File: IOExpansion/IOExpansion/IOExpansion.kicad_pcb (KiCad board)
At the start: 2 copper layers, 155 x 114 mm, 61 parts, among them J1 Mount_Hole_3.2mm_M3, J10 HEADER 2x20, J11 I2C_5V, J12 I2C_3V3, J13 I2C_ALT_Master, J14 I2C_Debug, J2 Mount_Hole_3.2mm_M3, J3 Mount_Hole_3.2mm_M3, J4 Mount_Hole_3.2mm_M3, J5 UART_5V, J6 GPIO_3V3, J7 RTC_SQW, J8 I2C_INT, J9 SPI _3V3, U1 MCP810-450, U10 PCA9641, U11 SC18IS602B, U12 PCA9517A, U13 PCA9517A, U14 MCP809-450, U15 LM3671_Breakout, U2 MCP809-315, U3 SG-8002DC, U4 PC16550D, U5 TXB0104_Breakout, U6 PCA9632DP1_Breakout, U7 GAL16V8, U8 SC18IM700, U9 PCF8523_Breakout

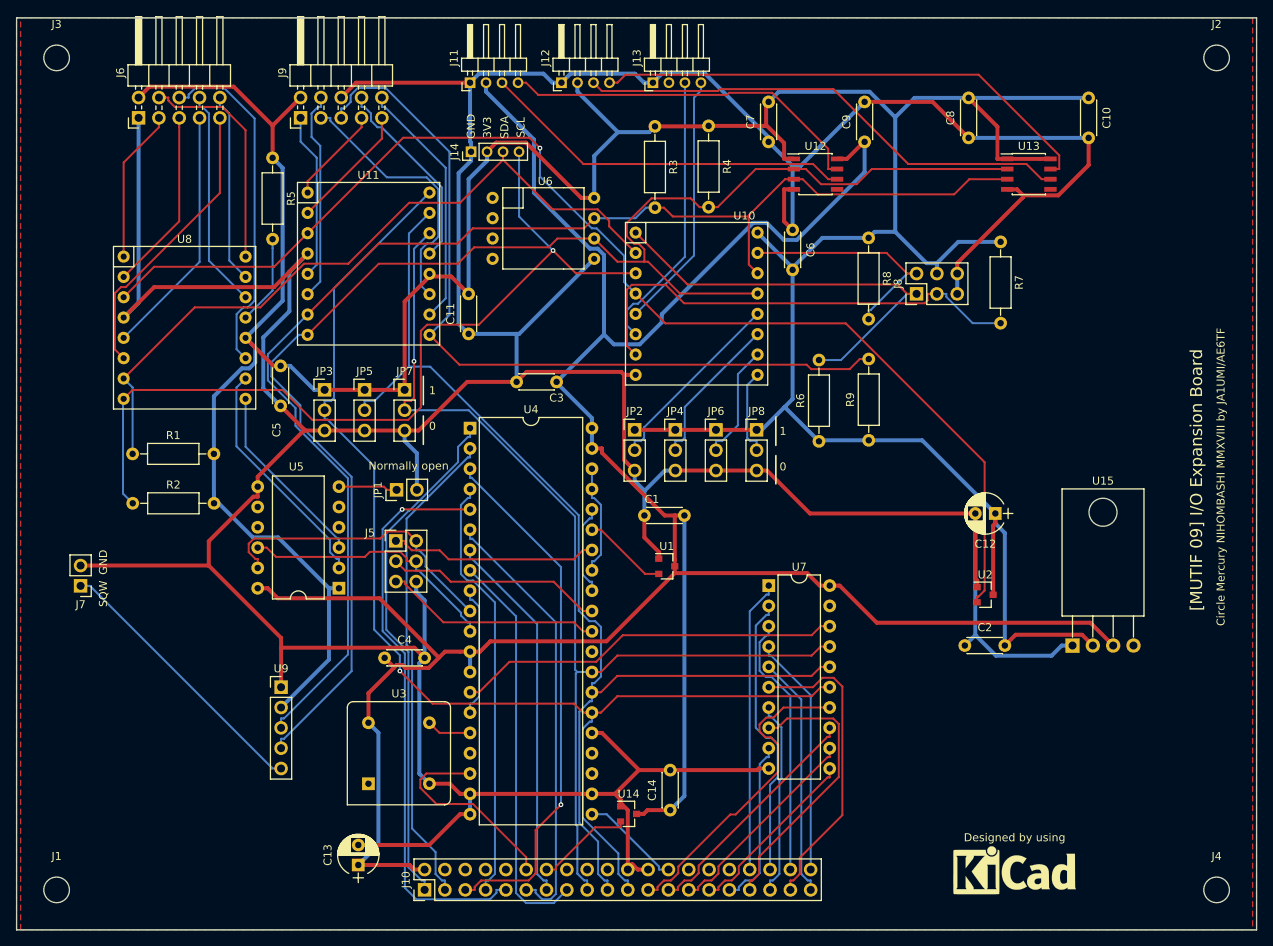
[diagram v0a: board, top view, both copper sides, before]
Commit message: Update files for MUTIF09 I/O Expansion Board (Revision 3). Functionality tests were completed on May 21, 2019.
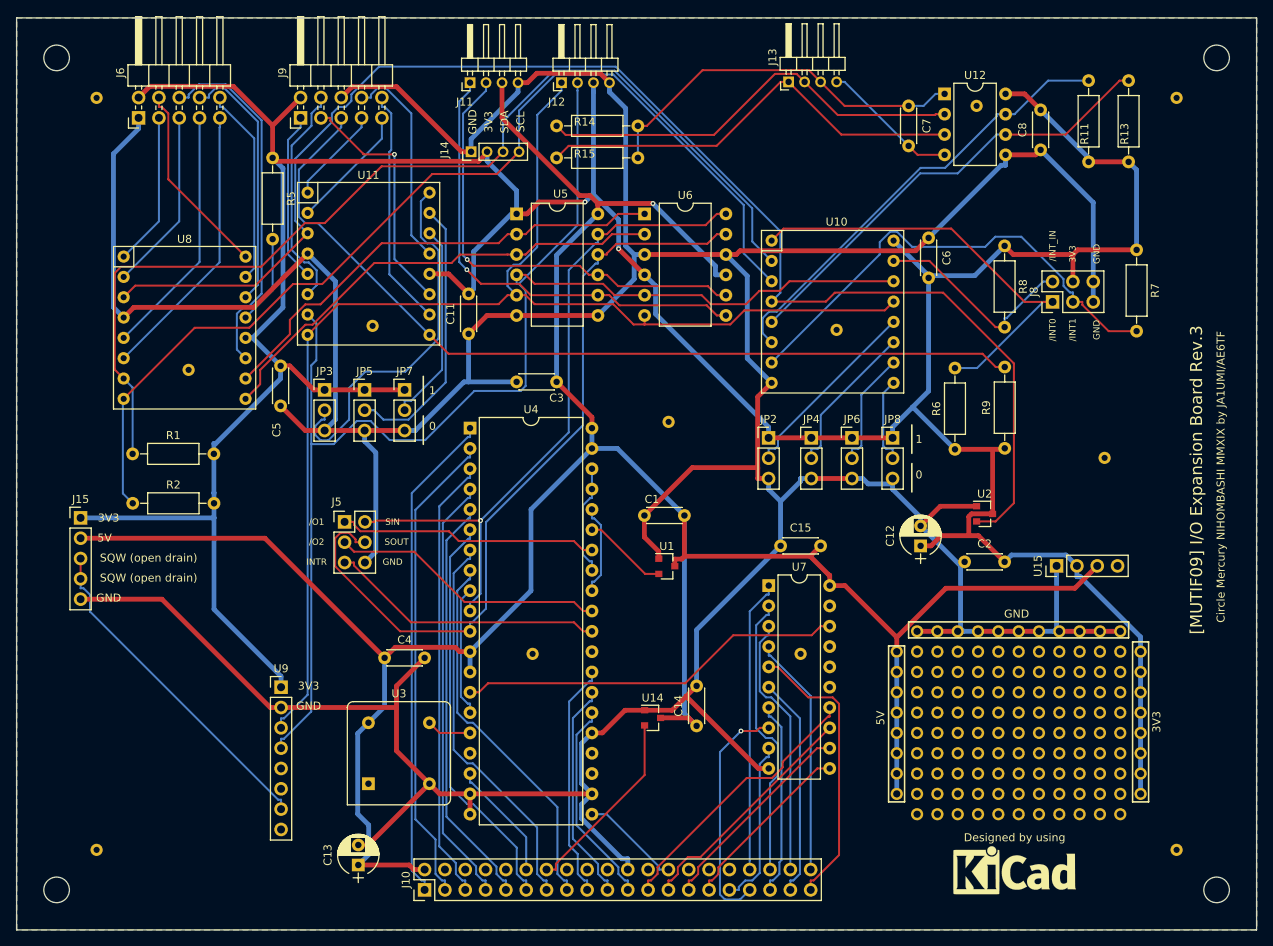
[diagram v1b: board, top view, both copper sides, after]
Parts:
- removed C10, C9: 0.1u, Capacitors_THT:C_Disc_D4.3mm_W1.9mm_P5.00mm
- removed J7: RTC_SQW, Pin_Headers:Pin_Header_Straight_1x02_Pitch2.54mm
- removed JP1: UART PassThru, Pin_Headers:Pin_Header_Straight_1x02_Pitch2.54mm
- removed R3, R4: 1.8K, Resistors_THT:R_Axial_DIN0207_L6.3mm_D2.5mm_P10.16mm_Horizontal
- removed U13: PCA9517A, Housings_SOIC:SOIC-8_3.9x4.9mm_Pitch1.27mm
- added C15: 0.1u, Capacitors_THT:C_Disc_D4.3mm_W1.9mm_P5.00mm, F.Cu at (145.5, 96.0)
- added J15: SQW_OUT, Pin_Headers:Pin_Header_Straight_1x05_Pitch2.54mm, F.Cu at (58.0, 92.5)
- added R11: 10K, Resistors_THT:R_Axial_DIN0207_L6.3mm_D2.5mm_P10.16mm_Horizontal, F.Cu at (184.0, 48.0)
- added R13: 10K, Resistors_THT:R_Axial_DIN0207_L6.3mm_D2.5mm_P10.16mm_Horizontal, F.Cu at (189.0, 48.0)
- added R14: R, Resistors_THT:R_Axial_DIN0207_L6.3mm_D2.5mm_P10.16mm_Horizontal, F.Cu at (117.5, 43.5)
- added R15: R, Resistors_THT:R_Axial_DIN0207_L6.3mm_D2.5mm_P10.16mm_Horizontal, F.Cu at (117.5, 47.5)
- added REF**: via, mylib:via, F.Cu at (94.5, 68.5)
- added REF**: via, mylib:via, F.Cu at (195.0, 134.0)
- added REF**: via, mylib:via, F.Cu at (195.0, 40.0)
- added REF**: via, mylib:via, F.Cu at (60.0, 40.0)
- added REF**: via, mylib:via, F.Cu at (170.0, 41.0)
- added REF**: via, mylib:via, F.Cu at (186.0, 85.0)
- added REF**: via, mylib:via, F.Cu at (131.5, 80.5)
- added REF**: via, mylib:via, F.Cu at (148.0, 109.5)
- added REF**: via, mylib:via, F.Cu at (152.5, 69.0)
- added REF**: via, mylib:via, F.Cu at (71.5, 74.0)
- added REF**: via, mylib:via, F.Cu at (114.5, 109.5)
- added REF**: via, mylib:via, F.Cu at (60.0, 134.0)
- added REF00: pad, mylib:pad, F.Cu at (162.6, 106.7)
- added REF01: pad, mylib:pad, F.Cu at (165.1, 106.7)
- added REF02: pad, mylib:pad, F.Cu at (167.6, 106.7)
- added REF03: pad, mylib:pad, F.Cu at (170.2, 106.7)
- added REF04: pad, mylib:pad, F.Cu at (172.7, 106.7)
- added REF05: pad, mylib:pad, F.Cu at (175.3, 106.7)
- added REF06: pad, mylib:pad, F.Cu at (177.8, 106.7)
- added REF07: pad, mylib:pad, F.Cu at (180.3, 106.7)
- added REF08: pad, mylib:pad, F.Cu at (182.9, 106.7)
- added REF09: pad, mylib:pad, F.Cu at (185.4, 106.7)
- added REF10: pad, mylib:pad, F.Cu at (188.0, 106.7)
- added REF100: pad, mylib:pad, F.Cu at (165.1, 129.5)
- added REF101: pad, mylib:pad, F.Cu at (167.6, 129.5)
- added REF102: pad, mylib:pad, F.Cu at (170.2, 129.5)
- added REF103: pad, mylib:pad, F.Cu at (172.7, 129.5)
- added REF104: pad, mylib:pad, F.Cu at (175.3, 129.5)
- added REF105: pad, mylib:pad, F.Cu at (177.8, 129.5)
- added REF106: pad, mylib:pad, F.Cu at (180.3, 129.5)
- added REF107: pad, mylib:pad, F.Cu at (182.9, 129.5)
- added REF108: pad, mylib:pad, F.Cu at (185.4, 129.5)
- added REF109: pad, mylib:pad, F.Cu at (188.0, 129.5)
- added REF11: pad, mylib:pad, F.Cu at (162.6, 109.2)
- added REF110: pad, mylib:pad, F.Cu at (160.0, 109.2)
- added REF111: pad, mylib:pad, F.Cu at (160.0, 111.8)
- added REF112: pad, mylib:pad, F.Cu at (160.0, 114.3)
- added REF113: pad, mylib:pad, F.Cu at (160.0, 116.8)
- added REF114: pad, mylib:pad, F.Cu at (160.0, 119.4)
- added REF115: pad, mylib:pad, F.Cu at (160.0, 121.9)
- added REF116: pad, mylib:pad, F.Cu at (160.0, 124.5)
- added REF117: pad, mylib:pad, F.Cu at (160.0, 127.0)
- added REF118: pad, mylib:pad, F.Cu at (190.5, 109.2)
- added REF119: pad, mylib:pad, F.Cu at (190.5, 111.8)
- added REF12: pad, mylib:pad, F.Cu at (165.1, 109.2)
- added REF120: pad, mylib:pad, F.Cu at (190.5, 114.3)
- added REF121: pad, mylib:pad, F.Cu at (190.5, 116.8)
- added REF122: pad, mylib:pad, F.Cu at (190.5, 119.4)
- added REF123: pad, mylib:pad, F.Cu at (190.5, 121.9)
- added REF124: pad, mylib:pad, F.Cu at (190.5, 124.5)
- added REF125: pad, mylib:pad, F.Cu at (190.5, 127.0)
- added REF13: pad, mylib:pad, F.Cu at (167.6, 109.2)
- added REF14: pad, mylib:pad, F.Cu at (170.2, 109.2)
- added REF15: pad, mylib:pad, F.Cu at (172.7, 109.2)
- added REF16: pad, mylib:pad, F.Cu at (175.3, 109.2)
- added REF17: pad, mylib:pad, F.Cu at (177.8, 109.2)
- added REF18: pad, mylib:pad, F.Cu at (180.3, 109.2)
- added REF19: pad, mylib:pad, F.Cu at (182.9, 109.2)
- added REF20: pad, mylib:pad, F.Cu at (185.4, 109.2)
- added REF21: pad, mylib:pad, F.Cu at (188.0, 109.2)
- added REF22: pad, mylib:pad, F.Cu at (162.6, 111.8)
- added REF23: pad, mylib:pad, F.Cu at (165.1, 111.8)
- added REF24: pad, mylib:pad, F.Cu at (167.6, 111.8)
- added REF25: pad, mylib:pad, F.Cu at (170.2, 111.8)
- added REF26: pad, mylib:pad, F.Cu at (172.7, 111.8)
- added REF27: pad, mylib:pad, F.Cu at (175.3, 111.8)
- added REF28: pad, mylib:pad, F.Cu at (177.8, 111.8)
- added REF29: pad, mylib:pad, F.Cu at (180.3, 111.8)
- added REF30: pad, mylib:pad, F.Cu at (182.9, 111.8)
- added REF31: pad, mylib:pad, F.Cu at (185.4, 111.8)
- added REF32: pad, mylib:pad, F.Cu at (188.0, 111.8)
- added REF33: pad, mylib:pad, F.Cu at (162.6, 114.3)
- added REF34: pad, mylib:pad, F.Cu at (165.1, 114.3)
- added REF35: pad, mylib:pad, F.Cu at (167.6, 114.3)
- added REF36: pad, mylib:pad, F.Cu at (170.2, 114.3)
- added REF37: pad, mylib:pad, F.Cu at (172.7, 114.3)
- added REF38: pad, mylib:pad, F.Cu at (175.3, 114.3)
- added REF39: pad, mylib:pad, F.Cu at (177.8, 114.3)
- added REF40: pad, mylib:pad, F.Cu at (180.3, 114.3)
- added REF41: pad, mylib:pad, F.Cu at (182.9, 114.3)
- added REF42: pad, mylib:pad, F.Cu at (185.4, 114.3)
- added REF43: pad, mylib:pad, F.Cu at (188.0, 114.3)
- added REF44: pad, mylib:pad, F.Cu at (162.6, 116.8)
- added REF45: pad, mylib:pad, F.Cu at (165.1, 116.8)
- added REF46: pad, mylib:pad, F.Cu at (167.6, 116.8)
- added REF47: pad, mylib:pad, F.Cu at (170.2, 116.8)
- added REF48: pad, mylib:pad, F.Cu at (172.7, 116.8)
- added REF49: pad, mylib:pad, F.Cu at (175.3, 116.8)
- added REF50: pad, mylib:pad, F.Cu at (177.8, 116.8)
- added REF51: pad, mylib:pad, F.Cu at (180.3, 116.8)
- added REF52: pad, mylib:pad, F.Cu at (182.9, 116.8)
- added REF53: pad, mylib:pad, F.Cu at (185.4, 116.8)
- added REF54: pad, mylib:pad, F.Cu at (188.0, 116.8)
- added REF55: pad, mylib:pad, F.Cu at (162.6, 119.4)
- added REF56: pad, mylib:pad, F.Cu at (165.1, 119.4)
- added REF57: pad, mylib:pad, F.Cu at (167.6, 119.4)
- added REF58: pad, mylib:pad, F.Cu at (170.2, 119.4)
- added REF59: pad, mylib:pad, F.Cu at (172.7, 119.4)
- added REF60: pad, mylib:pad, F.Cu at (175.3, 119.4)
- added REF61: pad, mylib:pad, F.Cu at (177.8, 119.4)
- added REF62: pad, mylib:pad, F.Cu at (180.3, 119.4)
- added REF63: pad, mylib:pad, F.Cu at (182.9, 119.4)
- added REF64: pad, mylib:pad, F.Cu at (185.4, 119.4)
- added REF65: pad, mylib:pad, F.Cu at (188.0, 119.4)
- added REF66: pad, mylib:pad, F.Cu at (162.6, 121.9)
- added REF67: pad, mylib:pad, F.Cu at (165.1, 121.9)
- added REF68: pad, mylib:pad, F.Cu at (167.6, 121.9)
- added REF69: pad, mylib:pad, F.Cu at (170.2, 121.9)
- added REF70: pad, mylib:pad, F.Cu at (172.7, 121.9)
- added REF71: pad, mylib:pad, F.Cu at (175.3, 121.9)
- added REF72: pad, mylib:pad, F.Cu at (177.8, 121.9)
- added REF73: pad, mylib:pad, F.Cu at (180.3, 121.9)
- added REF74: pad, mylib:pad, F.Cu at (182.9, 121.9)
- added REF75: pad, mylib:pad, F.Cu at (185.4, 121.9)
- added REF76: pad, mylib:pad, F.Cu at (188.0, 121.9)
- added REF77: pad, mylib:pad, F.Cu at (162.6, 124.5)
- added REF78: pad, mylib:pad, F.Cu at (165.1, 124.5)
- added REF79: pad, mylib:pad, F.Cu at (167.6, 124.5)
- added REF80: pad, mylib:pad, F.Cu at (170.2, 124.5)
- added REF81: pad, mylib:pad, F.Cu at (172.7, 124.5)
- added REF82: pad, mylib:pad, F.Cu at (175.3, 124.5)
- added REF83: pad, mylib:pad, F.Cu at (177.8, 124.5)
- added REF84: pad, mylib:pad, F.Cu at (180.3, 124.5)
- added REF85: pad, mylib:pad, F.Cu at (182.9, 124.5)
- added REF86: pad, mylib:pad, F.Cu at (185.4, 124.5)
- added REF87: pad, mylib:pad, F.Cu at (188.0, 124.5)
- added REF88: pad, mylib:pad, F.Cu at (162.6, 127.0)
- added REF89: pad, mylib:pad, F.Cu at (165.1, 127.0)
- added REF90: pad, mylib:pad, F.Cu at (167.6, 127.0)
- added REF91: pad, mylib:pad, F.Cu at (170.2, 127.0)
- added REF92: pad, mylib:pad, F.Cu at (172.7, 127.0)
- added REF93: pad, mylib:pad, F.Cu at (175.3, 127.0)
- added REF94: pad, mylib:pad, F.Cu at (177.8, 127.0)
- added REF95: pad, mylib:pad, F.Cu at (180.3, 127.0)
- added REF96: pad, mylib:pad, F.Cu at (182.9, 127.0)
- added REF97: pad, mylib:pad, F.Cu at (185.4, 127.0)
- added REF98: pad, mylib:pad, F.Cu at (188.0, 127.0)
- added REF99: pad, mylib:pad, F.Cu at (162.6, 129.5)
- J14: value I2C_Debug -> I2C_Debug_3V3
- J9: value SPI _3V3 -> SPI_3V3
- R1, R2: value 1.8K -> 10K
- U10: value PCA9641 -> PCA9641 (or PCA9541)
- U12: value PCA9517A -> ADuM1250; footprint Housings_SOIC:SOIC-8_3.9x4.9mm_Pitch1.27mm -> Housings_DIP:DIP-8_W7.62mm
- U15: footprint TO_SOT_Packages_THT:TO-220-4_Horizontal -> Pin_Headers:Pin_Header_Straight_1x04_Pitch2.54mm
- U5: value TXB0104_Breakout -> 4ch_Level_Shifter_BSS138
- U6: value PCA9632DP1_Breakout -> 4ch_Level_Shifter_BSS138(AKI); footprint ioexplib:PCA9632DP1_Breakout -> Housings_DIP:DIP-12_W10.16mm
- U9: value PCF8523_Breakout -> DS3231_Breakout; footprint Pin_Headers:Pin_Header_Straight_1x05_Pitch2.54mm -> Pin_Headers:Pin_Header_Straight_1x08_Pitch2.54mm
- moved U5 51.8 mm to (112.5, 54.5), turned to 0 degrees
- moved U6 19.1 mm to (128.5, 54.5)
- moved U12 19.0 mm to (166.0, 39.5)
- moved C7 18.1 mm to (161.5, 41.0), turned to 270 degrees
- moved C6 17.0 mm to (164.0, 57.5)
- moved J8 17.0 mm to (179.5, 65.5)
- moved JP4 17.0 mm to (149.3, 82.5)
- moved JP6 17.0 mm to (154.4, 82.5)
- moved JP8 17.0 mm to (159.5, 82.5)
- moved R6 17.0 mm to (167.3, 83.9)
- moved R7 17.0 mm to (190.0, 59.0)
- moved R8 17.0 mm to (173.5, 58.5)
- moved R9 17.0 mm to (173.5, 83.8)
- moved U10 17.0 mm to (152.0, 68.0)
- moved J13 17.0 mm to (146.5, 38.0)
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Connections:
- net /AD0 renamed /AB0
- net /AD1 renamed /AB1
- net /AD2 renamed /AB2
- net /AD3 renamed /AB3
- C7 pad 1: /GND -> Net-(C7-Pad1)
- C7 pad 2: /+3V3 -> Net-(C7-Pad2)
- J10 pad 24: /GND -> Net-(J10-Pad24)
- J11 pad 1: /GND -> /SCL_SLAVE_5V
- J11 pad 2: /+5V -> /SDA_SLAVE_5V
- J11 pad 3: Net-(J11-Pad3) -> /+5V
- J11 pad 4: Net-(J11-Pad4) -> /GND
- J12 pad 1: /GND -> /SCL_SLAVE
- J12 pad 2: /+3V3 -> /SDA_SLAVE
- J12 pad 3: Net-(J12-Pad3) -> /+3V3
- J12 pad 4: Net-(J12-Pad4) -> /GND
- J13 pad 1: /GND -> Net-(J13-Pad1)
- J13 pad 3: /SDA_MST1 -> Net-(C7-Pad1)
- J13 pad 4: /SCL_MST1 -> Net-(C7-Pad2)
- JP3 pad 2: /A2 -> /AS2
- JP5 pad 2: /A1 -> /AS1
- JP7 pad 2: /A0 -> /AS0
- U11 pad 14: /A0 -> /AS0
- U11 pad 15: /A1 -> /AS1
- U11 pad 16: /A2 -> /AS2
- U12 pad 1: /+3V3 -> Net-(C7-Pad1)
- U12 pad 2: /SCL_SLAVE -> Net-(J13-Pad2)
- U12 pad 3: /SDA_SLAVE -> Net-(J13-Pad1)
- U12 pad 4: /GND -> Net-(C7-Pad2)
- U12 pad 5: Net-(U12-Pad5) -> /GND
- U12 pad 6: Net-(J11-Pad3) -> /SCL_MST1
- U12 pad 7: Net-(J11-Pad4) -> /SDA_MST1
- U12 pad 8: /+5V -> /+3V3
- U5 pad 4: Net-(U5-Pad4) -> /SDA_SLAVE
- U5 pad 5: Net-(U5-Pad5) -> /SCL_SLAVE
- U5 pad 6: Net-(JP1-Pad1) -> /GND
- U5 pad 8: Net-(U5-Pad8) -> /SCL_SLAVE_5V
- U5 pad 9: Net-(U5-Pad9) -> /SDA_SLAVE_5V
- U6 pad 1: Net-(U6-Pad1) -> /TX
- U6 pad 2: Net-(U6-Pad2) -> /RX
- U6 pad 3: Net-(U6-Pad3) -> /GND
- U6 pad 4: Net-(U6-Pad4) -> /+3V3
- U6 pad 5: /GND -> /SDA_SLAVE
- U6 pad 7: /SDA_SLAVE -> /SCL_SLAVE_5V
- U6 pad 8: /+3V3 -> /SDA_SLAVE_5V
- U7 pad 15: /A2 -> Net-(U7-Pad15)
- U7 pad 16: /A1 -> Net-(U7-Pad16)
- U7 pad 17: /A0 -> Net-(U7-Pad17)
- U9 pad 1: /GND -> /+3V3
- U9 pad 2: /+3V3 -> /GND
- U9 pad 3: /SDA_SLAVE -> /SCL_SLAVE
- U9 pad 4: /SCL_SLAVE -> /SDA_SLAVE
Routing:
- net /A2: track 152.3 -> 26.0 mm, vias 1 -> 0
- net /A1: track 140.3 -> 27.9 mm
- net /A0: track 131.2 -> 29.7 mm, vias 1 -> 0
- net /SOUT: track 33.2 -> 99.6 mm
- net Net-(J12-Pad4): track 63.6 -> 0.00 mm
- net Net-(J12-Pad3): track 62.3 -> 0.00 mm
- net /SCL_SLAVE_5V: track 0.00 -> 59.1 mm, vias 0 -> 1
- net /SDA_SLAVE_5V: track 0.00 -> 57.7 mm, vias 0 -> 1
- net Net-(J13-Pad1): track 0.00 -> 55.2 mm
- net Net-(J13-Pad2): track 0.00 -> 54.3 mm
- net /SIN: track 37.5 -> 85.6 mm, vias 0 -> 1
- net Net-(C7-Pad1): track 0.00 -> 47.7 mm
- net /AS2: track 0.00 -> 47.0 mm
- net Net-(J11-Pad3): track 46.9 -> 0.00 mm
- net Net-(J11-Pad4): track 46.1 -> 0.00 mm
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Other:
- net class Power: trace_width 0.5 -> 0.6
- board text added: "/INT0"
- board text added: "/INT1"
- board text added: "/INT_IN"
- board text added: "/O1"
- board text added: "/O2"
- board text added: "5V"
- board text added: "Circle Mercury NIHOMBASHI MMXIX by JA1UMI/AE6TF"
- board text added: "INTR"
- board text added: "SIN"
- board text added: "SOUT"
- board text added: "SQW (open drain)"
- board text added: "[MUTIF09] I/O Expansion Board Rev.3"
- board text removed: "Circle Mercury NIHOMBASHI MMXVIII by JA1UMI/AE6TF"
- board text removed: "Normally open"
- board text removed: "SQW"
- board text removed: "[MUTIF 09] I/O Expansion Board"
